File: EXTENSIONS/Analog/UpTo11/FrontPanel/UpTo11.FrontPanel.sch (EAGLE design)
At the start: 2 parts

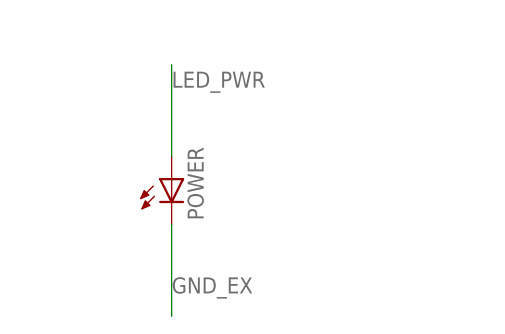
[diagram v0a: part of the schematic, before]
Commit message: Create UpTo11 Front Panel
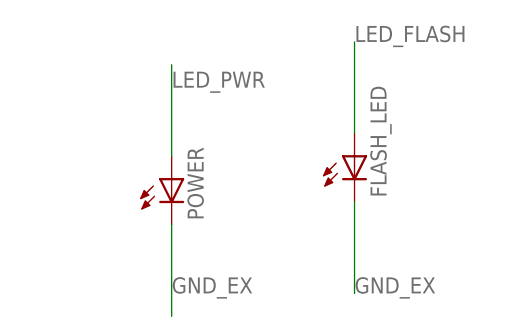
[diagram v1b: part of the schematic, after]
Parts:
- added FLASH_LED: (no value), adafruit:LED5MM
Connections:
- net GND_EX: now also FLASH_LED.C
- net LED_FLASH: now also FLASH_LED.A
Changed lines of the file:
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@@
 <classes>
 <class number="0" name="default" width="0" drill="0">
+<clearance class="0" value="0.205"/>
 </class>
 </classes>
@@
 <part name="FRONT_PANEL_INTERFACE" library="adafruit" deviceset="PINHD-1X6" device=""/>
 <part name="POWER" library="adafruit" deviceset="LED" device="SMT1206"/>
+<part name="FLASH_LED" library="adafruit" deviceset="LED" device="5MM"/>
 </parts>
 <sheets>
@@
 <instance part="FRONT_PANEL_INTERFACE" gate="A" x="-2.54" y="81.28" rot="R180"/>
 <instance part="POWER" gate="G$1" x="45.72" y="73.66"/>
+<instance part="FLASH_LED" gate="G$1" x="66.04" y="76.2"/>
 </instances>
 <busses>
@@
 <wire x1="0" y1="81.28" x2="15.24" y2="81.28" width="0.1524" layer="91"/>
 <label x="10.16" y="81.28" size="1.778" layer="95"/>
+</segment>
+<segment>
+<pinref part="FLASH_LED" gate="G$1" pin="A"/>
+<wire x1="66.04" y1="78.74" x2="66.04" y2="88.9" width="0.1524" layer="91"/>
+<label x="66.04" y="88.9" size="1.778" layer="95"/>
 </segment>
 </net>
@@
 <label x="45.72" y="60.96" size="1.778" layer="95"/>
 </segment>
+<segment>
+<pinref part="FLASH_LED" gate="G$1" pin="C"/>
+<wire x1="66.04" y1="71.12" x2="66.04" y2="60.96" width="0.1524" layer="91"/>
+<label x="66.04" y="60.96" size="1.778" layer="95"/>
+</segment>
 </net>

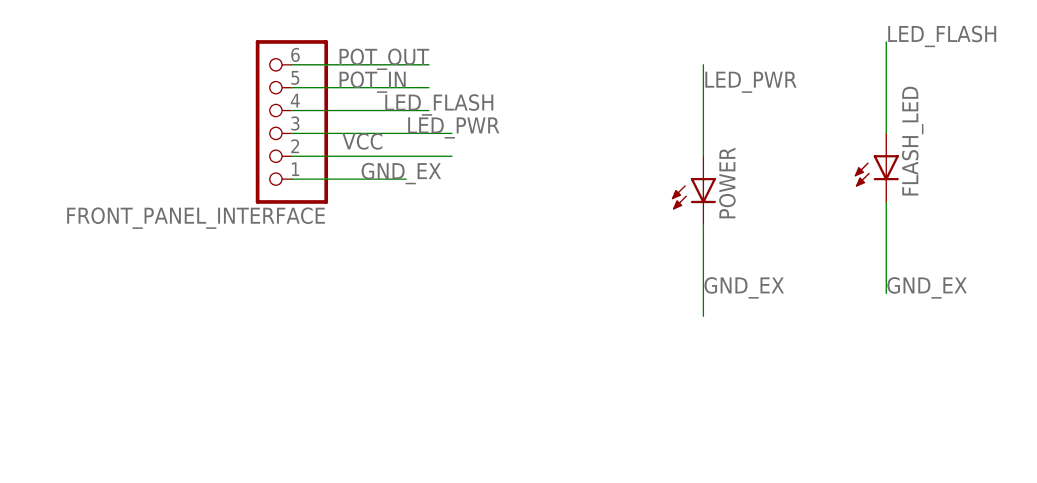
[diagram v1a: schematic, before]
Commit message: Create UpTo11 Front Panel
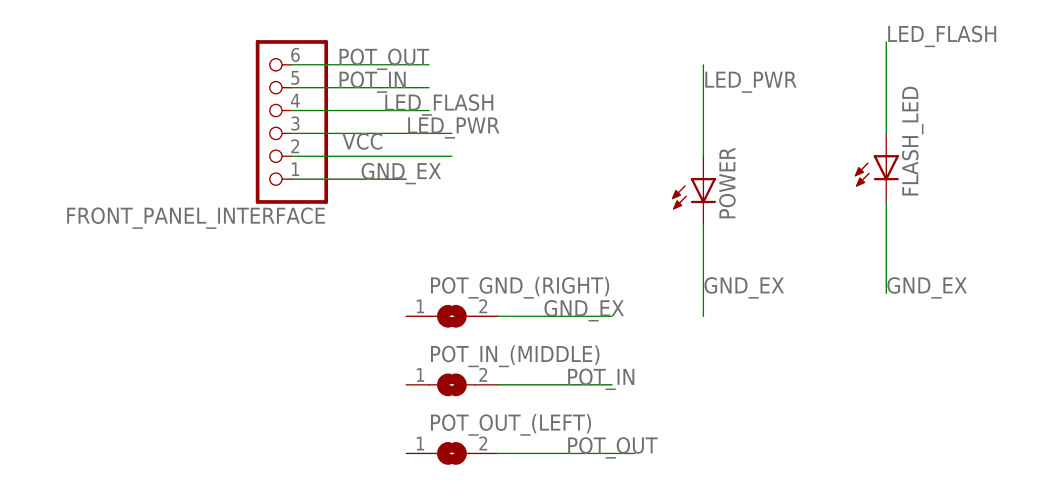
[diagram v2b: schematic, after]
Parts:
- added POT_GND_(RIGHT), POT_IN_(MIDDLE), POT_OUT_(LEFT): (no value), microbuilder:SOLDERJUMPERREFLOW
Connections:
- net GND_EX: now also POT_GND_(RIGHT).2
- net POT_IN: now also POT_IN_(MIDDLE).2
- net POT_OUT: now also POT_OUT_(LEFT).2
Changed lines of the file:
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@@
 <part name="POWER" library="adafruit" deviceset="LED" device="SMT1206"/>
 <part name="FLASH_LED" library="adafruit" deviceset="LED" device="5MM"/>
+<part name="POT_GND_(RIGHT)" library="microbuilder" deviceset="SOLDERJUMPER" device="REFLOW"/>
+<part name="POT_IN_(MIDDLE)" library="microbuilder" deviceset="SOLDERJUMPER" device="REFLOW"/>
+<part name="POT_OUT_(LEFT)" library="microbuilder" deviceset="SOLDERJUMPER" device="REFLOW"/>
 </parts>
 <sheets>
@@
 <instance part="POWER" gate="G$1" x="45.72" y="73.66"/>
 <instance part="FLASH_LED" gate="G$1" x="66.04" y="76.2"/>
+<instance part="POT_GND_(RIGHT)" gate="1" x="17.78" y="58.42"/>
+<instance part="POT_IN_(MIDDLE)" gate="1" x="17.78" y="50.8"/>
+<instance part="POT_OUT_(LEFT)" gate="1" x="17.78" y="43.18"/>
 </instances>
 <busses>
@@
 <label x="66.04" y="60.96" size="1.778" layer="95"/>
 </segment>
+<segment>
+<pinref part="POT_GND_(RIGHT)" gate="1" pin="2"/>
+<wire x1="22.86" y1="58.42" x2="35.56" y2="58.42" width="0.1524" layer="91"/>
+<label x="27.94" y="58.42" size="1.778" layer="95"/>
+</segment>
 </net>
 <net name="VCC" class="0">
@@
 <label x="5.08" y="83.82" size="1.778" layer="95"/>
 </segment>
+<segment>
+<pinref part="POT_IN_(MIDDLE)" gate="1" pin="2"/>
+<wire x1="22.86" y1="50.8" x2="35.56" y2="50.8" width="0.1524" layer="91"/>
+<label x="30.48" y="50.8" size="1.778" layer="95"/>
+</segment>
 </net>
 <net name="POT_OUT" class="0">
@@
 <label x="5.08" y="86.36" size="1.778" layer="95"/>
 </segment>
+<segment>
+<pinref part="POT_OUT_(LEFT)" gate="1" pin="2"/>
+<wire x1="22.86" y1="43.18" x2="38.1" y2="43.18" width="0.1524" layer="91"/>
+<label x="30.48" y="43.18" size="1.778" layer="95"/>
+</segment>
 </net>

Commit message: Create UpTo11 Front Panel
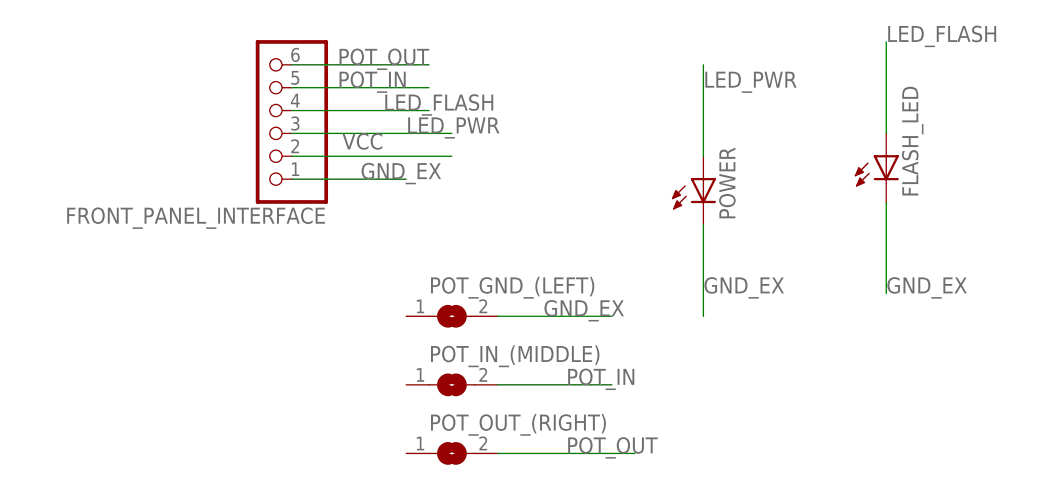
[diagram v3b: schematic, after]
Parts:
- renumbered POT_GND_(RIGHT) to POT_GND_(LEFT), POT_OUT_(LEFT) to POT_OUT_(RIGHT)
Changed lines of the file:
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@@
 <part name="POWER" library="adafruit" deviceset="LED" device="SMT1206"/>
 <part name="FLASH_LED" library="adafruit" deviceset="LED" device="5MM"/>
-<part name="POT_GND_(RIGHT)" library="microbuilder" deviceset="SOLDERJUMPER" device="REFLOW"/>
+<part name="POT_GND_(LEFT)" library="microbuilder" deviceset="SOLDERJUMPER" device="REFLOW"/>
 <part name="POT_IN_(MIDDLE)" library="microbuilder" deviceset="SOLDERJUMPER" device="REFLOW"/>
-<part name="POT_OUT_(LEFT)" library="microbuilder" deviceset="SOLDERJUMPER" device="REFLOW"/>
+<part name="POT_OUT_(RIGHT)" library="microbuilder" deviceset="SOLDERJUMPER" device="REFLOW"/>
 </parts>
 <sheets>
@@
 <instance part="POWER" gate="G$1" x="45.72" y="73.66"/>
 <instance part="FLASH_LED" gate="G$1" x="66.04" y="76.2"/>
-<instance part="POT_GND_(RIGHT)" gate="1" x="17.78" y="58.42"/>
+<instance part="POT_GND_(LEFT)" gate="1" x="17.78" y="58.42"/>
 <instance part="POT_IN_(MIDDLE)" gate="1" x="17.78" y="50.8"/>
-<instance part="POT_OUT_(LEFT)" gate="1" x="17.78" y="43.18"/>
+<instance part="POT_OUT_(RIGHT)" gate="1" x="17.78" y="43.18"/>
 </instances>
 <busses>
@@
 </segment>
 <segment>
-<pinref part="POT_GND_(RIGHT)" gate="1" pin="2"/>
+<pinref part="POT_GND_(LEFT)" gate="1" pin="2"/>
 <wire x1="22.86" y1="58.42" x2="35.56" y2="58.42" width="0.1524" layer="91"/>
 <label x="27.94" y="58.42" size="1.778" layer="95"/>
@@
 </segment>
 <segment>
-<pinref part="POT_OUT_(LEFT)" gate="1" pin="2"/>
+<pinref part="POT_OUT_(RIGHT)" gate="1" pin="2"/>
 <wire x1="22.86" y1="43.18" x2="38.1" y2="43.18" width="0.1524" layer="91"/>
 <label x="30.48" y="43.18" size="1.778" layer="95"/>
